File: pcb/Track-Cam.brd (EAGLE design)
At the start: 65 x 56 mm, 47 parts, among them IC1 STM32F042KT/M, IC2 BD6211F/M, IC3 BD6211F/M, P1 RASPI_BOARD_B+#_HC

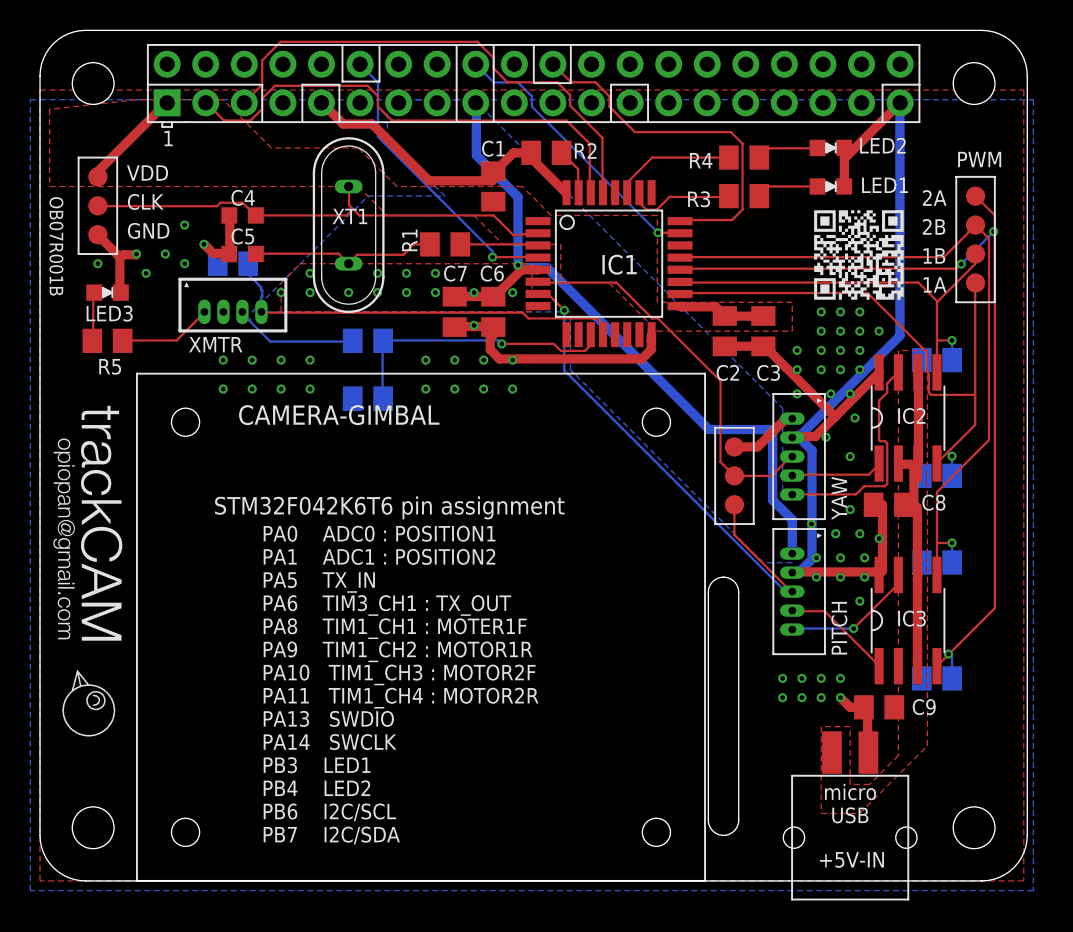
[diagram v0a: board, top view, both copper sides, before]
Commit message: change pcb design as connecting with Rasbery Pi by SPI
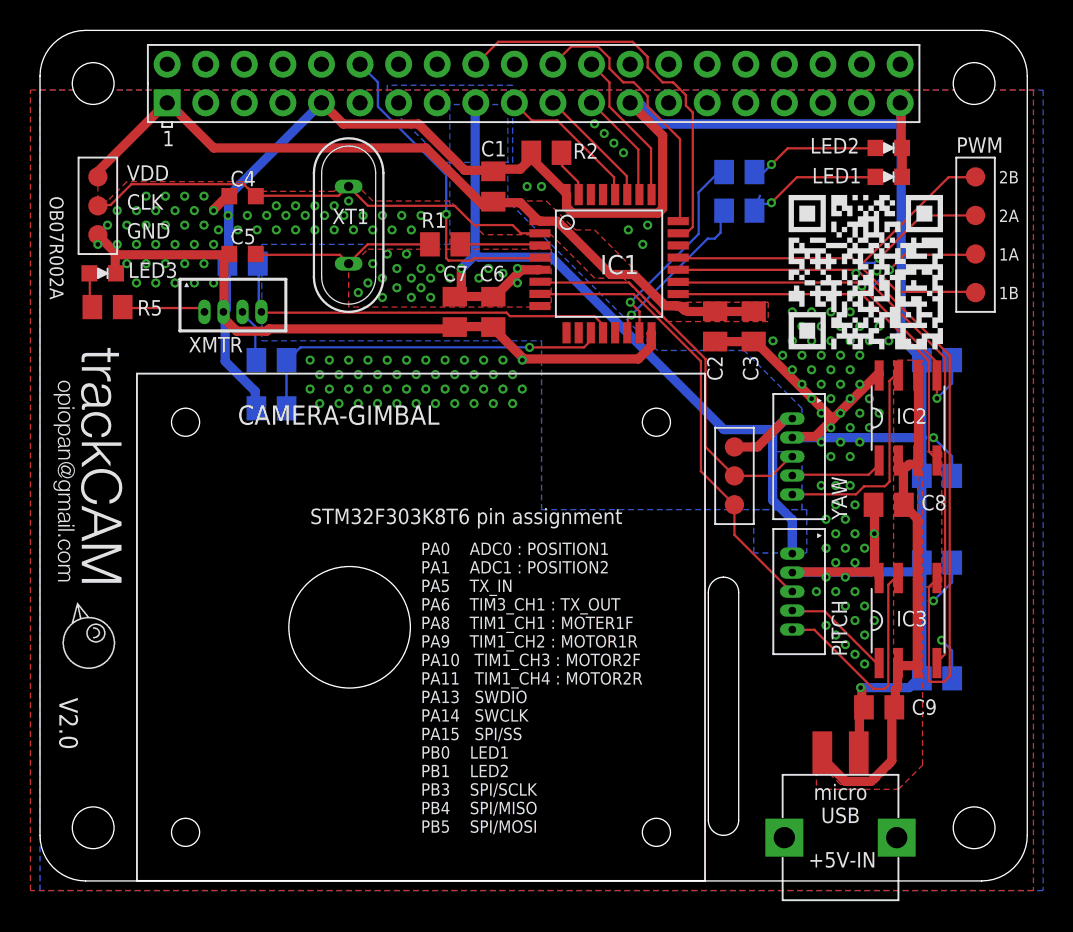
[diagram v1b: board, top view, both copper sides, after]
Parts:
- IC1: value STM32F042KT/M -> STM32F303K8T6
- moved R10 6.48 mm to (15.2, 34.3)
- moved R11 6.38 mm to (15.2, 31.1)
- moved U$1 4.44 mm to (0.95, 18.4)
- moved U$3 4.41 mm to (47.9, 33.7)
- moved LED1 3.86 mm to (55.9, 46.4)
- moved LED2 3.81 mm to (55.9, 48.3)
- moved U$2 3.81 mm to (0.64, 35.9)
- moved 2B 3.17 mm to (61.6, 46.4)
- moved 1B 2.54 mm to (61.6, 38.7)
- moved R5 2.22 mm to (4.45, 37.8)
- moved 1A 1.91 mm to (61.6, 41.3)
- moved LED3 1.31 mm to (4.13, 40.0)
- moved 2A 1.27 mm to (61.6, 43.8)
- moved C4 1.27 mm to (13.3, 45.1)
- moved R3 1.00 mm to (46.0, 44.1), flipped to the bottom, turned to 180 degrees
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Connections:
- removed net SCL: IC1.29, P1.5
- removed net SDA: IC1.30, P1.3
- new net SPI_MISO: IC1.27, P1.21
- new net SPI_MOSI: IC1.28, P1.19
- new net SPI_SCLK: IC1.26, P1.23
- new net SPI_SS: IC1.25, P1.24
- net LED1: now also IC1.14; no longer IC1.26
- net LED2: now also IC1.15; no longer IC1.27
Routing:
- net GND: track 123.9 -> 222.4 mm, vias 65 -> 191
- net VDD: track 12.5 -> 51.2 mm
- net SCL: track 33.2 -> 0.00 mm
- net SDA: track 32.4 -> 0.00 mm
- net MOTOR2_R: track 47.5 -> 63.6 mm
- net +5V: track 21.1 -> 35.3 mm
- net SPI_SS: track 0.00 -> 10.2 mm
- net SPI_MOSI: track 0.00 -> 9.75 mm
- net SPI_MISO: track 0.00 -> 8.08 mm
- net SWDIO: track 18.5 -> 26.3 mm, vias 1 -> 0
- net SPI_SCLK: track 0.00 -> 7.34 mm
- net MOTOR2-: track 8.86 -> 15.7 mm, vias 1 -> 0
- net SWCLK: track 23.8 -> 17.7 mm
- net N$8: track 4.10 -> 10.0 mm, vias 0 -> 1
- net LED2: track 8.04 -> 13.6 mm, vias 0 -> 1
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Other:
- board text added: "OB07R002A"
- board text added: "PA0 ADC0 : POSITION1 PA1 ADC1 : POSITION2 PA5 TX_IN PA6 TIM3_CH1 : TX_OUT PA8 TIM1_CH1 : MOTER1F PA9 TIM1_CH2 : MOTOR1R PA10 TIM1_CH3 : MOTOR2F PA11 TIM1_CH4 : MOTOR2R PA13 SWDIO PA14 SWCLK PA15 SPI/SS PB0 LED1 PB1 LED2 PB3 SPI/SCLK PB4 SPI/MISO PB5 SPI/MOSI"
- board text added: "STM32F303K8T6 pin assignment"
- board text added: "V2.0"
- board text removed: "OB07R001B"
- board text removed: "PA0 ADC0 : POSITION1 PA1 ADC1 : POSITION2 PA5 TX_IN PA6 TIM3_CH1 : TX_OUT PA8 TIM1_CH1 : MOTER1F PA9 TIM1_CH2 : MOTOR1R PA10 TIM1_CH3 : MOTOR2F PA11 TIM1_CH4 : MOTOR2R PA13 SWDIO PA14 SWCLK PB3 LED1 PB4 LED2 PB6 I2C/SCL PB7 I2C/SDA"
- board text removed: "STM32F042K6T6 pin assignment"

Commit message: improved pcb pattern
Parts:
- moved VDDA 2.25 mm to (46.0, 30.8)
- moved POS2 0.71 mm to (46.0, 24.1)
- moved POS1 0.71 mm to (46.0, 27.3)
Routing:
- net MOTOR1_POS: track 25.9 -> 25.1 mm
- net +3V3: track 59.0 -> 58.4 mm
- net GND: vias 191 -> 228

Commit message: optimize pcb design to suport 3D model
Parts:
- C1, C2, C3, C6, C7, C8, C9: device gen-discrete:SMD2012 -> gen-discrete2:SMD2012
- C4, C5: device gen-discrete:SMD1608 -> gen-discrete2:SMD1608
